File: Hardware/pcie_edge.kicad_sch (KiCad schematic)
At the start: 1 part, among them J1 Bus_PCI_Express_x1

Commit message: Trying to assign MGT lanes but I don't know how to do inter sheet connectivity yet
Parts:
- added C1, C2: 0.01uF, Capacitor_SMD:C_0402_1005Metric, symbol Device:C_Small
- added C3, C4: 0.22uF, Capacitor_SMD:C_0402_1005Metric, symbol Device:C_Small
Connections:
- net +3.3V: now reaches J1.A10 (+3.3V), J1.A9 (+3.3V), J1.B8 (+3.3V)
- net GND: now reaches J1.A12 (GND), J1.A15 (GND), J1.A18 (GND), J1.A4 (GND), J1.B13 (GND), J1.B16 (GND), J1.B18 (GND), J1.B4 (GND), J1.B7 (GND)
- net at J1.A13 (REFCLK+): now also C1.2
- net at J1.A14 (REFCLK-): now also C2.2
- net at J1.A16 (PERp0): now also C3.1
- net at J1.A17 (PERn0): now also C4.1
- net +12V: now reaches J1.A2 (+12V), J1.A3 (+12V), J1.B1 (+12V), J1.B2 (+12V), J1.B3 (+12V)
- net PCIE_TX_P: now reaches J1.B14 (PETp0)
- net PCIE_TX_N: now reaches J1.B15 (PETn0)
- new net PCIE_REFCLK_N: C2.1
- new net PCIE_REFCLK_P: C1.1
- new net PCIE_RX_N: C4.2
- new net PCIE_RX_P: C3.2

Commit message: Found the global labels
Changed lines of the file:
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@@
+		)
+	)
+	(global_label "PCIE_RX_N"
+		(shape output)
+		(at 226.06 107.95 0)
+		(fields_autoplaced yes)
+		(effects
+			(font
+				(size 1.27 1.27)
+			)
+			(justify left)
+		)
+		(property "Intersheetrefs" "${INTERSHEET_REFS}"
+			(at 239.0842 107.95 0)
+			(hide yes)
+			(show_name no)
+			(do_not_autoplace no)
+			(effects
+				(font
+					(size 1.27 1.27)
+				)
+				(justify left)
+			)
+		)
+	)
+	(global_label "PCIE_REFCLK_N"
+		(shape input)
+		(at 53.34 85.09 180)
+		(fields_autoplaced yes)
+		(effects
+			(font
+				(size 1.27 1.27)
+			)
+			(justify right)
+		)
+		(property "Intersheetrefs" "${INTERSHEET_REFS}"
+			(at 35.7196 85.09 0)
+			(hide yes)
+			(show_name no)
+			(do_not_autoplace no)
+			(effects
+				(font
+					(size 1.27 1.27)
+				)
+				(justify right)
+			)
+		)
+	)
+	(global_label "PCIE_RX_P"
+		(shape output)
+		(at 226.06 105.41 0)
+		(fields_autoplaced yes)
+		(effects
+			(font
+				(size 1.27 1.27)
+			)
+			(justify left)
+		)
+		(property "Intersheetrefs" "${INTERSHEET_REFS}"
+			(at 239.0237 105.41 0)
+			(hide yes)
+			(show_name no)
+			(do_not_autoplace no)
+			(effects
+				(font
+					(size 1.27 1.27)
+				)
+				(justify left)
+			)
+		)
+	)
+	(global_label "PCIE_REFCLK_P"
+		(shape input)
+		(at 53.34 82.55 180)
+		(fields_autoplaced yes)
+		(effects
+			(font
+				(size 1.27 1.27)
+			)
+			(justify right)
+		)
+		(property "Intersheetrefs" "${INTERSHEET_REFS}"
+			(at 35.7801 82.55 0)
+			(hide yes)
+			(show_name no)
+			(do_not_autoplace no)
+			(effects
+				(font
+					(size 1.27 1.27)
+				)
+				(justify right)
+			)
+		)
+	)
+	(global_label "PCIE_TX_N"
+		(shape input)
+		(at 88.9 107.95 180)
+		(fields_autoplaced yes)
+		(effects
+			(font
+				(size 1.27 1.27)
+			)
+			(justify right)
+		)
+		(property "Intersheetrefs" "${INTERSHEET_REFS}"
+			(at 76.1782 107.95 0)
+			(hide yes)
+			(show_name no)
+			(do_not_autoplace no)
+			(effects
+				(font
+					(size 1.27 1.27)
+				)
+				(justify right)
+			)
+		)
+	)
+	(global_label "PCIE_TX_P"
+		(shape input)
+		(at 88.9 105.41 180)
+		(fields_autoplaced yes)
+		(effects
+			(font
+				(size 1.27 1.27)
+			)
+			(justify right)
+		)
+		(property "Intersheetrefs" "${INTERSHEET_REFS}"
+			(at 76.2387 105.41 0)
+			(hide yes)
+			(show_name no)
+			(do_not_autoplace no)
+			(effects
+				(font
+					(size 1.27 1.27)
+				)
+				(justify right)
+			)
 		)
 	)

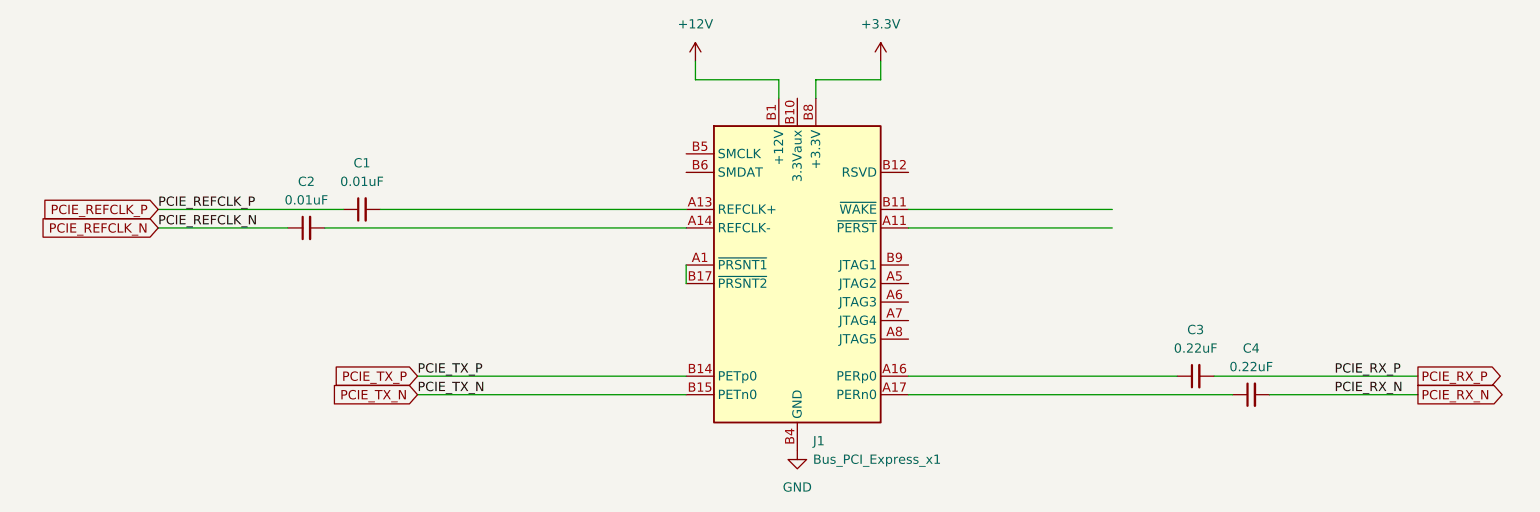
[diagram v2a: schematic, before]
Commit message: PCIE TX and RX swapped
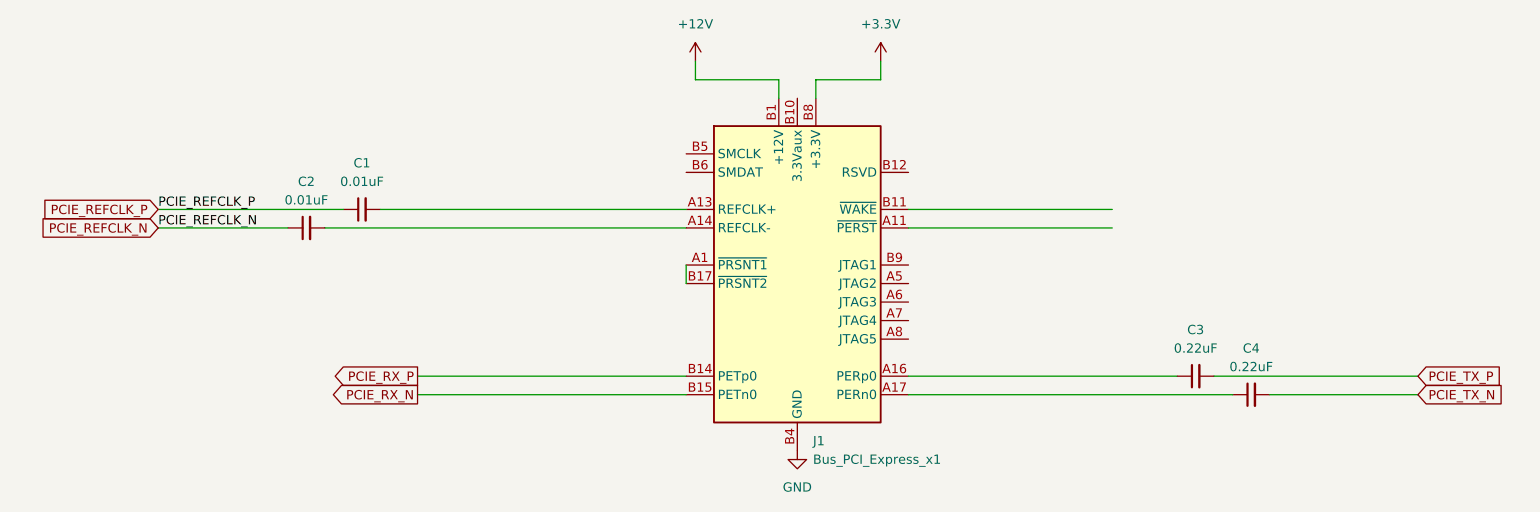
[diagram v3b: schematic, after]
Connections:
- net PCIE_RX_N: now also J1.B15 (PETn0); no longer C4.2
- net PCIE_RX_P: now also J1.B14 (PETp0); no longer C3.2
- net PCIE_TX_N: now also C4.2; no longer J1.B15 (PETn0)
- net PCIE_TX_P: now also C3.2; no longer J1.B14 (PETp0)
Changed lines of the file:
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@@
-		)
-	)
-	(label "PCIE_RX_P"
-		(at 214.63 105.41 0)
-		(effects
-			(font
-				(size 1.27 1.27)
-			)
-			(justify left bottom)
-		)
-	)
-	(label "PCIE_TX_N"
-		(at 88.9 107.95 0)
-		(effects
-			(font
-				(size 1.27 1.27)
-			)
-			(justify left bottom)
-		)
-	)
-	(label "PCIE_RX_N"
-		(at 214.63 107.95 0)
-		(effects
-			(font
-				(size 1.27 1.27)
-			)
-			(justify left bottom)
 		)
 	)
@@
 		)
 	)
-	(label "PCIE_TX_P"
-		(at 88.9 105.41 0)
-		(effects
-			(font
-				(size 1.27 1.27)
-			)
-			(justify left bottom)
-		)
-	)
-	(global_label "PCIE_RX_N"
-		(shape output)
+	(global_label "PCIE_TX_N"
+		(shape input)
 		(at 226.06 107.95 0)
 		(fields_autoplaced yes)
@@
 		)
 		(property "Intersheetrefs" "${INTERSHEET_REFS}"
-			(at 239.0842 107.95 0)
+			(at 238.7818 107.95 0)
 			(hide yes)
 			(show_name no)
@@
 		)
 	)
-	(global_label "PCIE_RX_P"
-		(shape output)
+	(global_label "PCIE_TX_P"
+		(shape input)
 		(at 226.06 105.41 0)
 		(fields_autoplaced yes)
@@
 		)
 		(property "Intersheetrefs" "${INTERSHEET_REFS}"
-			(at 239.0237 105.41 0)
+			(at 238.7213 105.41 0)
 			(hide yes)
 			(show_name no)
@@
 		)
 	)
-	(global_label "PCIE_TX_N"
-		(shape input)
+	(global_label "PCIE_RX_N"
+		(shape output)
 		(at 88.9 107.95 180)
 		(fields_autoplaced yes)
@@
 		)
 		(property "Intersheetrefs" "${INTERSHEET_REFS}"
-			(at 76.1782 107.95 0)
+			(at 75.8758 107.95 0)
 			(hide yes)
 			(show_name no)
@@
 		)
 	)
-	(global_label "PCIE_TX_P"
-		(shape input)
+	(global_label "PCIE_RX_P"
+		(shape output)
 		(at 88.9 105.41 180)
 		(fields_autoplaced yes)
@@
 		)
 		(property "Intersheetrefs" "${INTERSHEET_REFS}"
-			(at 76.2387 105.41 0)
+			(at 75.9363 105.41 0)
 			(hide yes)
 			(show_name no)

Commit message: Trying new fanout technology
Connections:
- net EDGE_REFCLK_N: now reaches C2.2, J1.A14 (REFCLK-)
- net EDGE_REFCLK_P: now reaches C1.2, J1.A13 (REFCLK+)
- net EDGE_TX_P: now reaches C3.1, J1.A16 (PERp0)
- net EDGE_TX_N: now reaches C4.1, J1.A17 (PERn0)
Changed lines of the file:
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@@
+		)
+	)
+	(label "EDGE_TX_P"
+		(at 168.91 105.41 0)
+		(effects
+			(font
+				(size 1.27 1.27)
+			)
+			(justify left bottom)
+		)
+	)
+	(label "EDGE_TX_N"
+		(at 168.91 107.95 0)
+		(effects
+			(font
+				(size 1.27 1.27)
+			)
+			(justify left bottom)
+		)
+	)
+	(label "EDGE_REFCLK_P"
+		(at 92.71 82.55 0)
+		(effects
+			(font
+				(size 1.27 1.27)
+			)
+			(justify left bottom)
 		)
 	)
@@
 		(effects
 			(font
+				(size 1.27 1.27)
+			)
+			(justify left bottom)
+		)
+	)
+	(label "EDGE_REFCLK_N"
+		(at 92.71 85.09 0)
+		(effects
+			(font
